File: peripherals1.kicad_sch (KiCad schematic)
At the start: 39 parts, among them Q1 Q_NMOS_GSD, SW4 SW_Push, SW5 SW_Push, SW6 SW_Push, SW7 SW_Push, U7 TSDP343xx

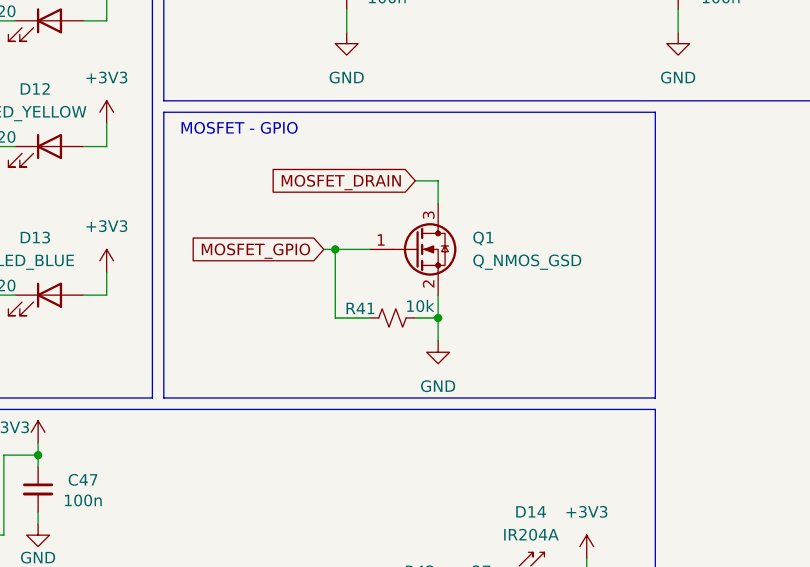
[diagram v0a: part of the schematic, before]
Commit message: feat: adds testpoints
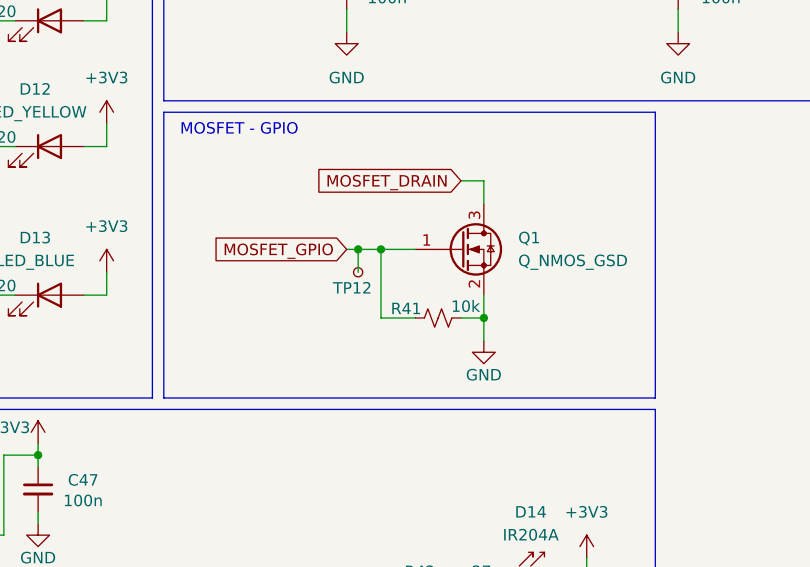
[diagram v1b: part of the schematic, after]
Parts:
- added TP12: TestPoint_Small, TestPoint:TestPoint_Pad_D1.0mm, symbol Connector:TestPoint_Small
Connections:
- net MOSFET_GPIO: now also TP12.1
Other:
- moved on the sheet: Q1, R41

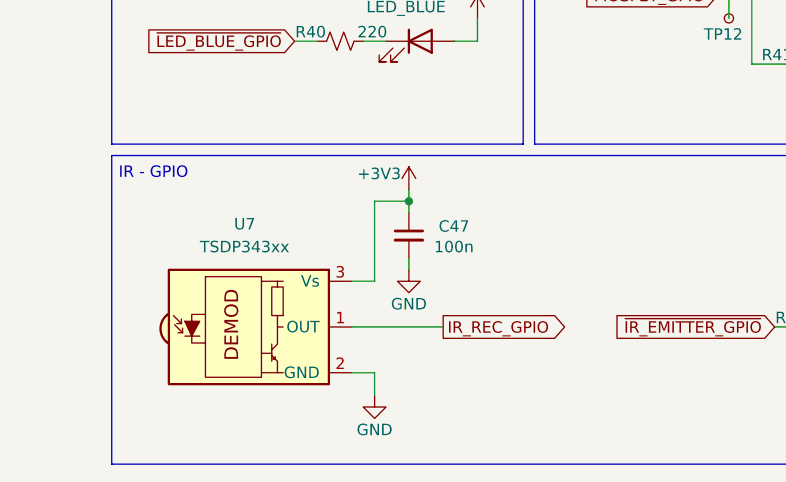
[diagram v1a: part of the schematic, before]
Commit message: feat:  adds requested components
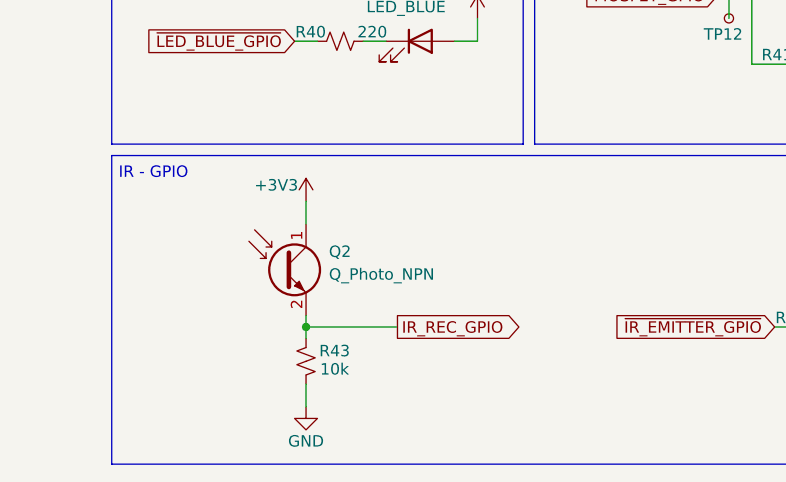
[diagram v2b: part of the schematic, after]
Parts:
- removed C47: 100n, Capacitor_SMD:C_0402_1005Metric, symbol Device:C_Small
- removed U7: TSDP343xx, OptoDevice:Vishay_MOLD-3Pin, symbol Interface_Optical:TSDP343xx
- added Q2: Q_Photo_NPN, peripherals1:TO-18-2, symbol Device:Q_Photo_NPN
- added R43: 10k, Resistor_SMD:R_0402_1005Metric, symbol Device:R_Small_US
- SW4, SW5, SW6, SW7: footprint microcontroller:SMD Button -> Button_Switch_THT:SW_PUSH_6mm_H4.3mm; MPN PTS636SM43SMTR LFS -> 1825910-6
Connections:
- net +3V3: now also Q2.1 (C)
- net GND: now also R43.1
- net IR_REC_GPIO: now also Q2.2 (E), R43.2

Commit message: wip: placement
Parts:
- added Q5: T2N7002AK,LM, Package_TO_SOT_SMD:SOT-23, symbol Transistor_FET:T2N7002AK
- added R56: 10k, Resistor_SMD:R_0402_1005Metric, symbol Device:R_Small_US
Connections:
- net +3V3: now also BZ1.1 (+), R35.2
- net BUZZER_GPIO: now also Q5.1 (G), R56.1; no longer R35.1
- net GND: now also Q5.2 (S), R56.2; no longer BZ1.2 (-)
- new net: BZ1.2 (-), Q5.3 (D), R35.1
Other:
- moved on the sheet: BZ1, R35

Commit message: wip: adds more routing
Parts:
- removed R39: 500, Resistor_SMD:R_0402_1005Metric, symbol Device:R_Small_US
- removed RV2: R_Pot_US, Potentiometer_THT:Potentiometer_Vishay_148-149_Single_Horizontal, symbol Device:R_Potentiometer_US
- D6: renamed from D9; value WS2812B -> FZ2812-5050
- renumbered C41 to C37, C42 to C38, C43 to C39, C44 to C40, C45 to C41, C46 to C42, D13 to D10, D14 to D11, D10 to D7, D11 to D8, D12 to D9, Q5 to Q1, Q1 to Q2, Q2 to Q3, R27 to R20, R28 to R21, R29 to R22, R30 to R23, R31 to R24, R32 to R25, R33 to R26, R34 to R27, R35 to R28, R36 to R29, R37 to R30, R56 to R31, R38 to R32, R40 to R33, R41 to R34, R42 to R35, R43 to R36, SW4 to SW2, SW5 to SW3, SW6 to SW4, SW7 to SW5, TP12 to TP11
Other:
- note added: "Potentiometer - ADC"
- note removed: "Potentiometers - ADC"

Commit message: refac: changes IR emitter
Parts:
- D11: value IR204A -> INL-3AHIR15; footprint Diode_SMD:D_0603_1608Metric -> LED_THT:LED_D3.0mm_IRBlack; MPN B13V1IR--20C000114U1930 -> INL-3AHIR15
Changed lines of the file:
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@@
 			)
 		)
-		(property "Value" "IR204A"
+		(property "Value" "INL-3AHIR15"
 			(at 123.317 158.75 0)
 			(effects
@@
 			)
 		)
-		(property "Footprint" "Diode_SMD:D_0603_1608Metric"
+		(property "Footprint" "LED_THT:LED_D3.0mm_IRBlack"
 			(at 124.46 159.385 0)
 			(effects
@@
 			)
 		)
-		(property "Datasheet" "https://www.digikey.com.br/en/products/detail/harvatek-corporation/B13V1IR-20C000114U1930/13574162?s=N4IgTCBcDaIEIEYDMA1BBJASgWm2ADAML4kIIAsAqggJxL4gC6AvkA"
+		(property "Datasheet" "https://www.digikey.com.br/pt/products/detail/inolux/INL-3AHIR15/10384794"
 			(at 123.19 163.83 0)
 			(effects
@@
 			)
 		)
-		(property "Description" "Infrared LED , 3mm LED package"
+		(property "Description" "THROUGH HOLE / STANDARD 3MM T1"
 			(at 124.46 163.83 0)
 			(effects
@@
 			)
 		)
-		(property "MPN" "B13V1IR--20C000114U1930"
+		(property "MPN" "INL-3AHIR15"
 			(at 124.46 163.83 0)
 			(effects

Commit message: fix: fixes schematic errors and some layout errors
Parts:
- BZ1: footprint Buzzer_Beeper:Buzzer_TDK_PS1240P02BT_D12.2mm_H6.5mm -> peripherals1:PS1440P02BT
- Q2: value Q_NMOS_GSD -> FDN327N
- R25, R30, R32, R33: MPN ERJ-2RKF2202X -> RC0402JR-13220RL
- R29: value 500 -> 100; MPN RT0402FRE07500RL -> ERJ-2RKF1000X
- RV1: footprint Potentiometer_THT:Potentiometer_Vishay_148-149_Single_Horizontal -> Potentiometer_THT:Potentiometer_Piher_T-16H_Single_Horizontal
- SW2, SW3, SW4, SW5: footprint Button_Switch_THT:SW_PUSH_6mm_H4.3mm -> peripherals1:SW_1825910-6-4; symbol Switch:SW_Push -> peripherals1:switch_button
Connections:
- net BUTTON1_GPIO: now also SW2.3; no longer SW2.2
- net BUTTON2_GPIO: now also SW3.3; no longer SW3.2
- net BUTTON3_GPIO: now also SW4.3; no longer SW4.2
- net BUTTON4_GPIO: now also SW5.3; no longer SW5.2
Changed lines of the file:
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@@
 			)
 		)
-		(property "Datasheet" "https://www.digikey.com.br/en/products/detail/panasonic-electronic-components/ERJ-2RKF2202X/1746152"
+		(property "Datasheet" "https://www.digikey.com.br/en/products/detail/yageo/RC0402JR-13220RL/14008194"
 			(at 60.96 115.57 0)
 			(effects
@@
 			)
 		)
-		(property "MPN" "ERJ-2RKF2202X"
+		(property "MPN" "RC0402JR-13220RL"
 			(at 60.96 115.57 90)
 			(effects
@@
 	)
 	(symbol
-		(lib_id "Switch:SW_Push")
+		(lib_id "peripherals1:switch_button")
 		(at 130.81 92.71 0)
 		(unit 1)
@@
 		(fields_autoplaced yes)
 		(property "Reference" "SW5"
-			(at 130.81 85.09 0)
+			(at 130.81 83.82 0)
 			(effects
 				(font
@@
 		)
 		(property "Value" "SW_Push"
-			(at 130.81 87.63 0)
+			(at 130.81 86.36 0)
 			(effects
 				(font
@@
 			)
 		)
-		(property "Footprint" "Button_Switch_THT:SW_PUSH_6mm_H4.3mm"
-			(at 130.81 87.63 0)
+		(property "Footprint" "peripherals1:SW_1825910-6-4"
+			(at 130.81 92.71 0)
 			(effects
 				(font
@@
 		)
 		(property "Datasheet" "https://www.digikey.com/en/products/detail/te-connectivity-alcoswitch-switches/1825910-6/1632536"
-			(at 130.81 87.63 0)
+			(at 130.81 92.71 0)
 			(effects
 				(font
@@
 		(pin "1"
 		)
+		(pin "3"
+		)
+		(pin "4"
+		)
 		(instances
 			(project "zbook"
@@
 			)
 		)
-		(property "Datasheet" "https://www.digikey.com.br/en/products/detail/panasonic-electronic-components/ERJ-2RKF2202X/1746152"
+		(property "Datasheet" "https://www.digikey.com.br/en/products/detail/yageo/RC0402JR-13220RL/14008194"
 			(at 60.96 86.36 0)
 			(effects
@@
 			)
 		)
-		(property "MPN" "ERJ-2RKF2202X"
+		(property "MPN" "RC0402JR-13220RL"
 			(at 60.96 86.36 90)
 			(effects
@@
 	)
 	(symbol
-		(lib_id "Switch:SW_Push")
+		(lib_id "peripherals1:switch_button")
 		(at 130.81 59.69 0)
 		(unit 1)
@@
 		(fields_autoplaced yes)
 		(property "Reference" "SW3"
-			(at 130.81 52.07 0)
+			(at 130.81 50.8 0)
 			(effects
 				(font
@@
 		)
 		(property "Value" "SW_Push"
-			(at 130.81 54.61 0)
+			(at 130.81 53.34 0)
 			(effects
 				(font
@@
 			)
 		)
-		(property "Footprint" "Button_Switch_THT:SW_PUSH_6mm_H4.3mm"
-			(at 130.81 54.61 0)
+		(property "Footprint" "peripherals1:SW_1825910-6-4"
+			(at 130.81 59.69 0)
 			(effects
 				(font
@@
 		)
 		(property "Datasheet" "https://www.digikey.com/en/products/detail/te-connectivity-alcoswitch-switches/1825910-6/1632536"
-			(at 130.81 54.61 0)
+			(at 130.81 59.69 0)
 			(effects
 				(font
@@
 		(pin "1"
 		)
+		(pin "4"
+		)
+		(pin "3"
+		)
 		(instances
 			(project "zbook"
@@
 			)
 		)
-		(property "Footprint" "Potentiometer_THT:Potentiometer_Vishay_148-149_Single_Horizontal"
+		(property "Footprint" "Potentiometer_THT:Potentiometer_Piher_T-16H_Single_Horizontal"
 			(at 224.79 96.52 0)
 			(effects
@@
 	)
 	(symbol
-		(lib_id "Switch:SW_Push")
+		(lib_id "peripherals1:switch_button")
 		(at 93.98 92.71 0)
 		(unit 1)
@@
 		(fields_autoplaced yes)
 		(property "Reference" "SW4"
-			(at 93.98 85.09 0)
+			(at 93.98 83.82 0)
 			(effects
 				(font
@@
 		)
 		(property "Value" "SW_Push"
-			(at 93.98 87.63 0)
+			(at 93.98 86.36 0)
 			(effects
 				(font
@@
 			)
 		)
-		(property "Footprint" "Button_Switch_THT:SW_PUSH_6mm_H4.3mm"
-			(at 93.98 87.63 0)
+		(property "Footprint" "peripherals1:SW_1825910-6-4"
+			(at 93.98 92.71 0)
 			(effects
 				(font
@@
 		)
 		(property "Datasheet" "https://www.digikey.com/en/products/detail/te-connectivity-alcoswitch-switches/1825910-6/1632536"
-			(at 93.98 87.63 0)
+			(at 93.98 92.71 0)
 			(effects
 				(font
@@
 		(pin "1"
 		)
+		(pin "4"
+		)
+		(pin "3"
+		)
 		(instances
 			(project "zbook"
@@
 	)
 	(symbol
-		(lib_id "Switch:SW_Push")
+		(lib_id "peripherals1:switch_button")
 		(at 93.98 59.69 0)
 		(unit 1)
@@
 		(fields_autoplaced yes)
 		(property "Reference" "SW2"
-			(at 93.98 52.07 0)
+			(at 93.98 50.8 0)
 			(effects
 				(font
@@
 		)
 		(property "Value" "SW_Push"
-			(at 93.98 54.61 0)
+			(at 93.98 53.34 0)
 			(effects
 				(font
@@
 			)
 		)
-		(property "Footprint" "Button_Switch_THT:SW_PUSH_6mm_H4.3mm"
-			(at 93.98 54.61 0)
+		(property "Footprint" "peripherals1:SW_1825910-6-4"
+			(at 93.98 59.69 0)
 			(effects
 				(font
@@
 		)
 		(property "Datasheet" "https://www.digikey.com/en/products/detail/te-connectivity-alcoswitch-switches/1825910-6/1632536"
-			(at 93.98 54.61 0)
+			(at 93.98 59.69 0)
 			(effects
 				(font
@@
 		(pin "1"
 		)
+		(pin "3"
+		)
+		(pin "4"
+		)
 		(instances
 			(project "zbook"
@@
 			)
 		)
-		(property "Footprint" "Buzzer_Beeper:Buzzer_TDK_PS1240P02BT_D12.2mm_H6.5mm"
+		(property "Footprint" "peripherals1:PS1440P02BT"
 			(at 194.945 87.63 90)
 			(effects
@@
 			)
 		)
-		(property "Value" "500"
+		(property "Value" "100"
 			(at 237.236 95.504 90)
 			(effects
@@
 			)
 		)
-		(property "Datasheet" "https://www.digikey.com.br/en/products/detail/yageo/RT0402FRE07500RL/17011324"
+		(property "Datasheet" "https://www.digikey.com.br/en/products/detail/panasonic-electronic-components/ERJ-2RKF1000X/192080"
 			(at 233.68 96.52 0)
 			(effects
@@
 			)
 		)
-		(property "MPN" "RT0402FRE07500RL"
+		(property "MPN" "ERJ-2RKF1000X"
 			(at 233.68 96.52 90)
 			(effects
@@
 			)
 		)
-		(property "Value" "Q_NMOS_GSD"
+		(property "Value" "FDN327N"
 			(at 121.92 128.2699 0)
 			(effects
@@
 			)
 		)
-		(property "Datasheet" "https://www.digikey.com.br/en/products/detail/panasonic-electronic-components/ERJ-2RKF2202X/1746152"
+		(property "Datasheet" "https://www.digikey.com.br/en/products/detail/yageo/RC0402JR-13220RL/14008194"
 			(at 60.96 132.08 0)
 			(effects
@@
 			)
 		)
-		(property "MPN" "ERJ-2RKF2202X"
+		(property "MPN" "RC0402JR-13220RL"
 			(at 60.96 132.08 90)
 			(effects
@@
 			)
 		)
-		(property "Datasheet" "https://www.digikey.com.br/en/products/detail/panasonic-electronic-components/ERJ-2RKF2202X/1746152"
+		(property "Datasheet" "https://www.digikey.com.br/en/products/detail/yageo/RC0402JR-13220RL/14008194"
 			(at 60.96 101.6 0)
 			(effects
@@
 			)
 		)
-		(property "MPN" "ERJ-2RKF2202X"
+		(property "MPN" "RC0402JR-13220RL"
 			(at 60.96 101.6 90)
 			(effects
